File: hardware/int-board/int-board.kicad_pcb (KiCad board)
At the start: 2 copper layers, 59 x 85 mm, 33 parts, among them J1 PTSM 0,5/4-HH-2,5-THR, J2 PTSM 0,5/4-HH-2,5-THR, J3 PTSM 0,5/4-HH-2,5-THR, J4 PTSM 0,5/4-HH-2,5-THR, J5 Pi 40-pin socket, J6 PTSM 0,5/5-HH-2,5-THR, J7 PTSM 0,5/4-HH-2,5-THR, J8 SP-C SP-E COM, J9 GPIO breakout, U1 LTV-847, U2 LTV-847, U3 LTV-847

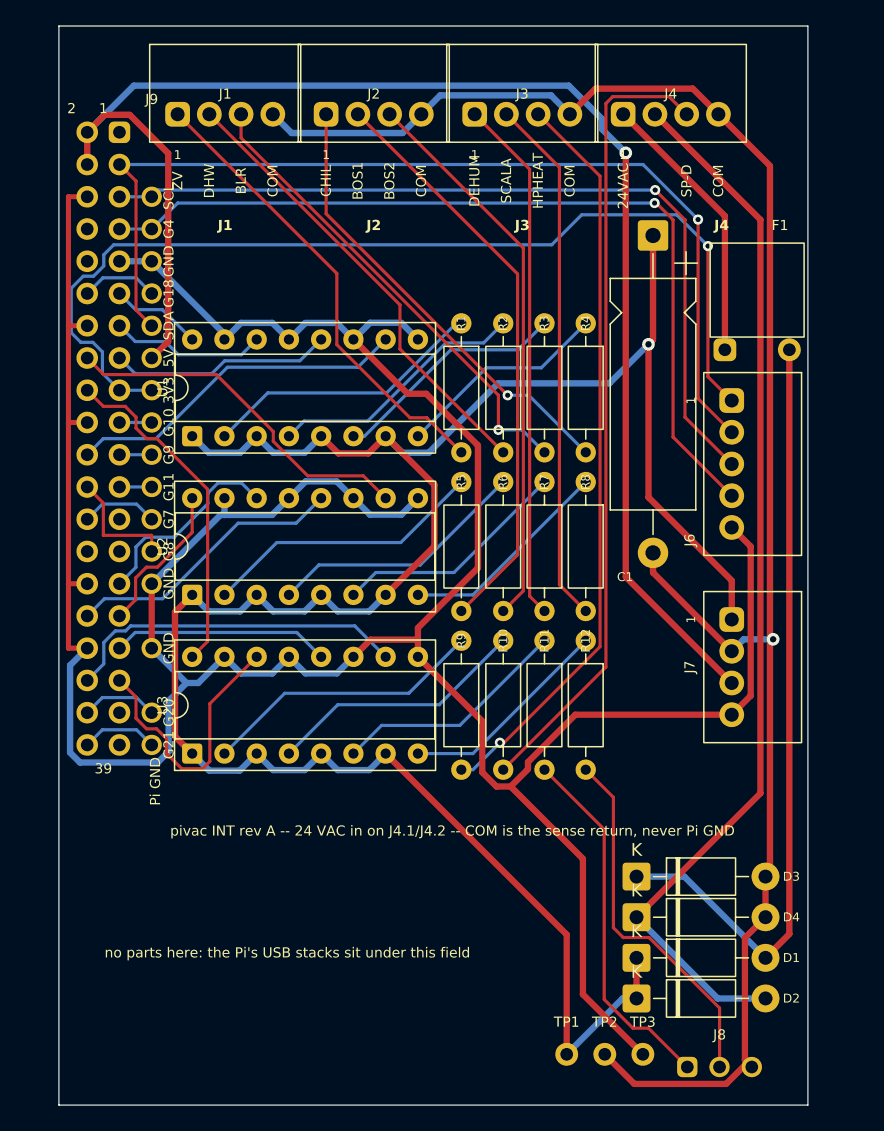
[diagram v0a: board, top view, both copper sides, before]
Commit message: Rev B plan: Pi supply on EXT, GH link, every channel on a plug (#214)
* Rev B plan: the Pi's supply moves to the EXT board, GH link, every channel on a plug

Rev A left the Pi on a wall adapter and put the 24 VAC entry on INT, which cost
two plug positions and forced HPCOOL onto the J8 pigtail whose loose connector
was the one fault at the 2026-09-26 cutover. Rev B moves the entry, the PTC, the
bridge and the reservoir to EXT's mid field, adds an isolated Traco TMR 12-4811WI
there, and feeds the Pi's own USB-C by a pigtail from a 2-pin XH header, so the
Pi's input protection stays in circuit and header pins 2 and 4 carry nothing.
VS and COM come back to INT over a 7-way JST GH link that replaces the PTSM
J6/J7 pair and latches after the boards are seated. J4 then takes HPCOOL, DHWX
and SP-E, J8 goes away, the optocoupler sockets shift right to clear the J9
breakout, and both boards get a DL title block.

The plan doc carries the circuit, the link pin map, the plug map, the EXT
positions, the parts list with distributor links and the path to the OSH Park
order. The SVG is the layout for review at 8 px per mm; hardware/dl-monogram.svg
is the mark's source for the KiCad footprint. The PCB plan's power section and
open items now state the rev B position.

Co-Authored-By: Claude Fable 5.1 <noreply@anthropic.com>

* Rev B plan: component index for both boards, PTSM edge offsets, link header at the rib

The plan now names every reference designator on both boards with its part,
body size, position and purpose, states how each PTSM header meets its board
edge (pin row 5.4 mm behind the entry face, from the Phoenix drawing the
footprint is built from: INT plugs 1.55 mm inside, EXT sockets and J3 1.7 mm
outside), and carries the carried-over parts alongside the new ones. EXT's J1
moves down to y 46.5-58.5 so it does not sit opposite INT's J6 in the opening.
The layout SVG draws the PTSM bodies at those offsets and J1 at its new place.

Co-Authored-By: Claude Fable 5.1 <norepl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
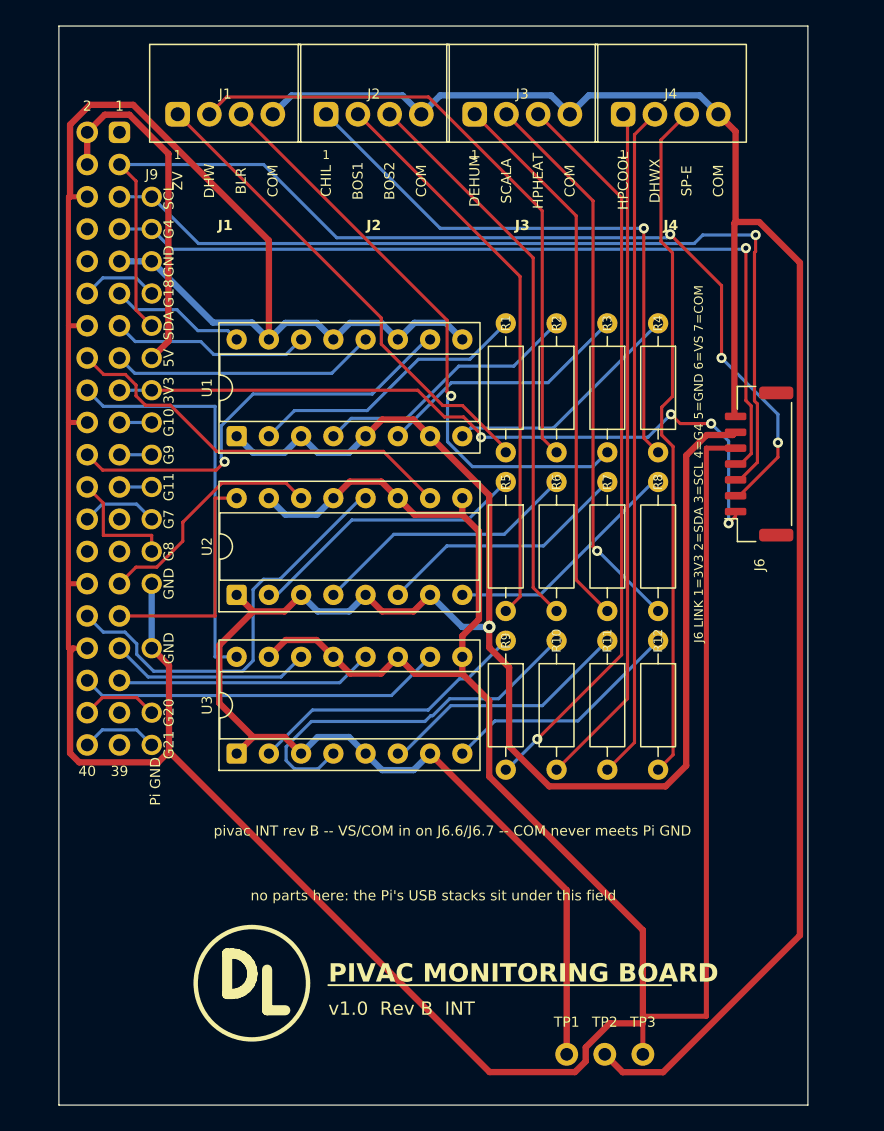
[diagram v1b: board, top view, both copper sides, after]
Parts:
- removed C1: 100u 63V axial, CP_Axial_L18.0mm_D6.5mm_P25.00mm_Horizontal
- removed D1, D2, D3, D4: 1N4007, D_DO-41_SOD81_P10.16mm_Horizontal
- removed F1: PTC 0.1A 60V, pivac:PTC_Radial_P5.08_Flat
- removed J7: PTSM 0,5/4-HH-2,5-THR, pivac:PTSM_0.5_4-HH-2.5-THR
- removed J8: SP-C SP-E COM, pivac:Pads_3x1
- J6: value PTSM 0,5/5-HH-2,5-THR -> GH SM07B link to EXT; footprint pivac:PTSM_0.5_5-HH-2.5-THR -> JST_GH_SM07B-GHS-TB_1x07-1MP_P1.25mm_Horizontal
- moved R12 5.70 mm to (47.2, 48.4)
- moved R4 5.70 mm to (47.2, 23.4)
- moved R8 5.70 mm to (47.2, 35.9)
- moved R11 4.95 mm to (43.2, 48.4)
- moved R3 4.95 mm to (43.2, 23.4)
- moved R7 4.95 mm to (43.2, 35.9)
- moved R10 4.20 mm to (39.2, 48.4)
- moved R2 4.20 mm to (39.2, 23.4)
- moved R6 4.20 mm to (39.2, 35.9)
- moved R1 3.50 mm to (35.2, 23.4)
- moved R5 3.50 mm to (35.2, 35.9)
- moved R9 3.50 mm to (35.2, 48.4)
- moved U1 3.50 mm to (14.0, 32.3)
- moved U2 3.50 mm to (14.0, 44.8)
- moved U3 3.50 mm to (14.0, 57.3)
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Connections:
- J4 pad 1: ACR -> S_HPCOOL
- J4 pad 2: ACC -> S_DHWX
- J4 pad 3: S_SP-D -> S_SP-E
- R10 pad 2: S_SP-D -> S_HPCOOL
- R11 pad 2: S_SP-C -> S_DHWX
- U3 pad 12: GPIO13 -> GPIO19
- U3 pad 14: GPIO19 -> GPIO13
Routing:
- net +5V: track 119.2 -> 27.4 mm, vias 1 -> 0
- net ACC: track 83.5 -> 0.00 mm
- net GND: track 260.9 -> 329.4 mm
- net S_SP-D: track 63.0 -> 0.00 mm
- net ACF: track 61.5 -> 0.00 mm
- net S_HPCOOL: track 0.00 -> 54.1 mm
- net S_DHWX: track 0.00 -> 53.2 mm
- net S_SP-C: track 28.8 -> 0.00 mm
- net S_SP-E: track 29.0 -> 54.1 mm
- net ACR: track 21.9 -> 0.00 mm
- net 3V3: track 79.7 -> 58.9 mm, vias 1 -> 4
- net S_DHW: track 36.2 -> 50.0 mm
- net GPIO12: track 22.3 -> 33.1 mm
- net S_CHIL: track 36.1 -> 46.9 mm
- net K10: track 20.6 -> 30.3 mm
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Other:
- board text added: "40"
- board text added: "DHWX"
- board text added: "HPCOOL"
- board text added: "J6 LINK 1=3V3 2=SDA 3=SCL 4=G4 5=GND 6=VS 7=COM"
- board text added: "PIVAC MONITORING BOARD"
- board text added: "SP-E"
- board text added: "pivac INT rev B -- VS/COM in on J6.6/J6.7 -- COM never meets Pi GND"
- board text added: "v1.0 Rev B INT"
- board text removed: "24VAC"
- board text removed: "LINK 3V3 SDA SCL G4 GND"
- board text removed: "PWR VS COM 5V GND"
- board text removed: "SP-D"
- board text removed: "pivac INT rev A -- 24 VAC in on J4.1/J4.2 -- COM is the sense return, never Pi GND"
